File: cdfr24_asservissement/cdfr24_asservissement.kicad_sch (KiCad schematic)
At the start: 64 parts, among them J1 Connecteur batterie, J10 Free Connecteur, J11 Conn_01x02, J12 Conn_01x02, J13 Connecteur Odométrie, J14 Conn_ST_STDC14, J2 Conn_01x03, J3 Conn_01x05, J4 Connecteur Programmation, J5 Conn_01x03, J6 Connecteur Odométrie, J7 Conn_01x03, Q13 Q_NMOS_GDS, U1 LM317_SOT-223, U3 STM32F401RCTx, U4 LMR16020PDDA, U4 LSM6DSL, Y1 Crystal_GND24

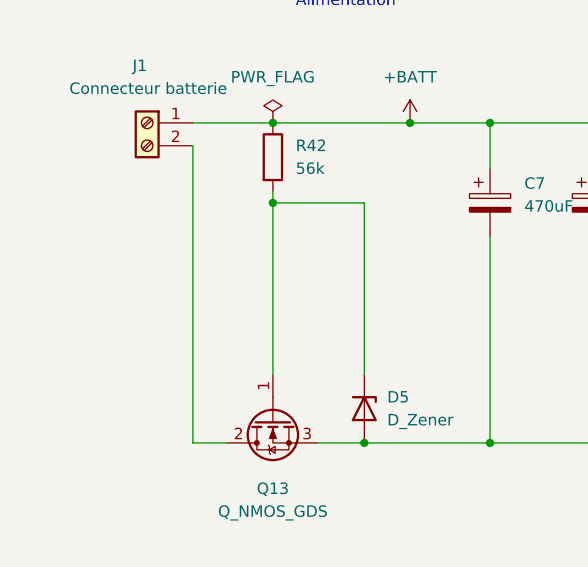
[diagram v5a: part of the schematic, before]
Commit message: correction Routage
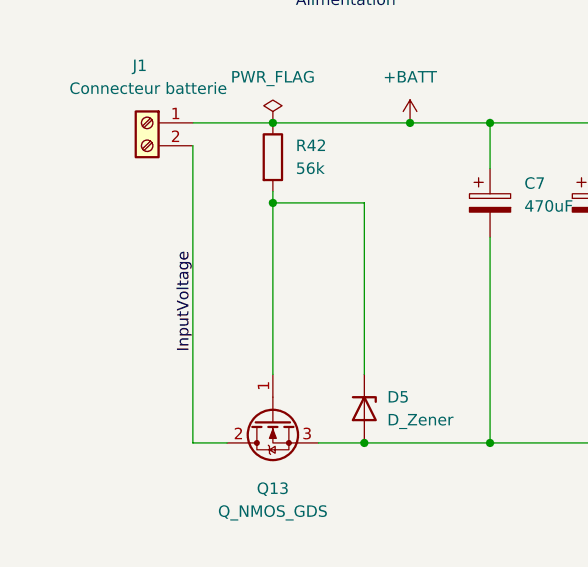
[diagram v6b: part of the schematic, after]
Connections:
- net InputVoltage: now reaches J1.2 (Pin_2), Q13.2 (D)
